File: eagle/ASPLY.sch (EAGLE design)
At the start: 69 parts, among them IC1 MC78L05ABP, IC2 TINY45, K1 Light, K2 Fan1, K3 Fan2, K4 Fan3, P1 MOLEX, T1 2SC1815, T2 2SC1815, T3 2SC1815, T4 2SC1815

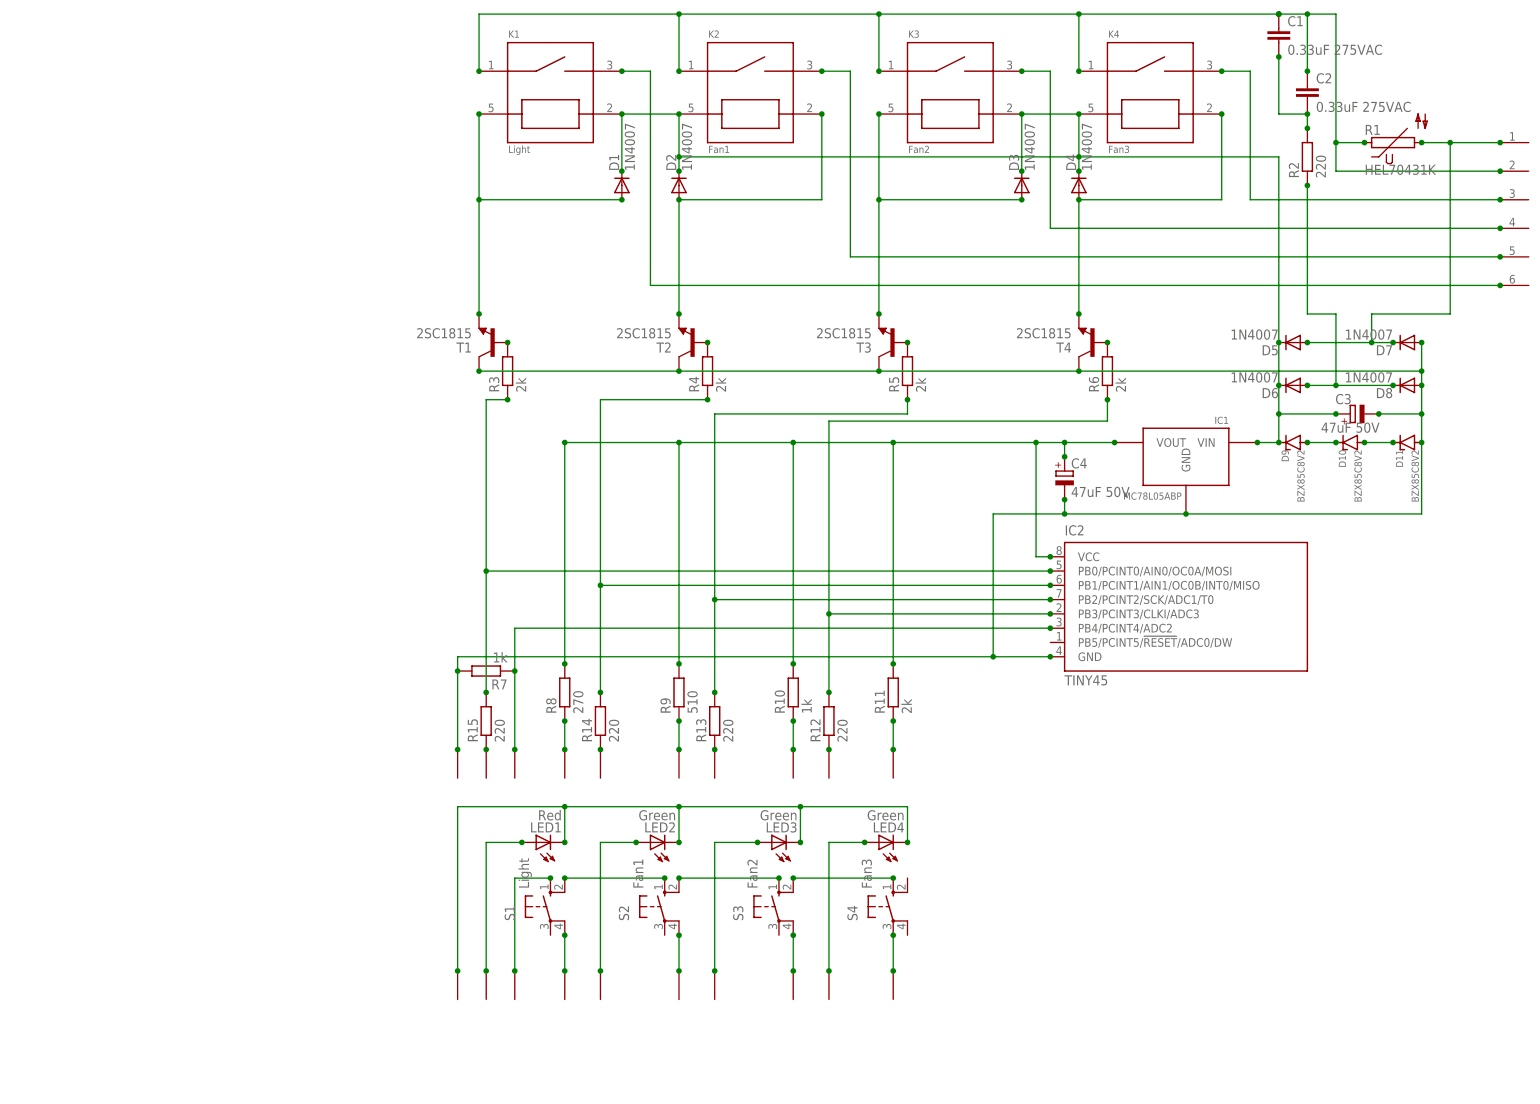
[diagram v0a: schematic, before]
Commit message: New HW revision:
- Split LED and transistor manage
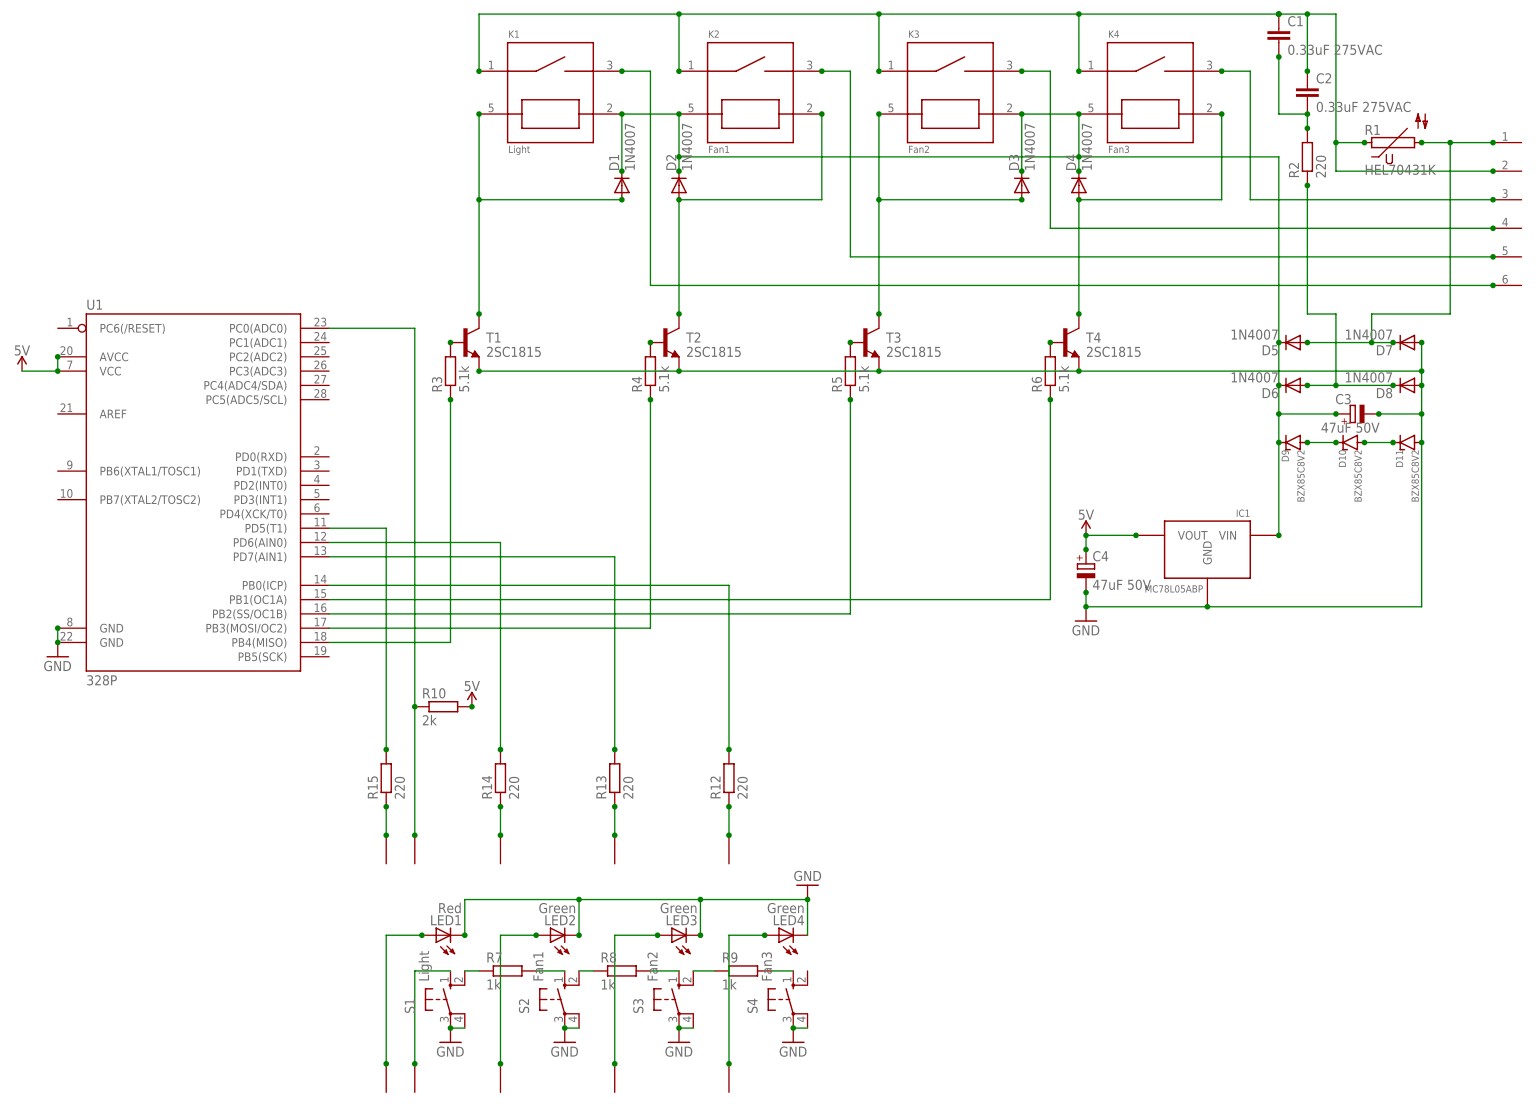
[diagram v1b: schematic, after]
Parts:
- removed IC2: TINY45, atmel:TINY13-20PU
- removed R11: 2k, rcl:R-EU_0204/7
- removed U$10, U$11, U$12, U$15, U$17, U$19, U$2, U$4, U$6, U$9: PIN, ASPLY:PIN
- added U1: 328P, SparkFun-IC-Microcontroller:ATMEGA328P_PDIP
- R10: value 1k -> 2k
- R3, R4, R5, R6: value 2k -> 5.1k
- R8: value 270 -> 1k
- R9: value 510 -> 1k
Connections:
- net N$1 renamed 220V
- net N$25 renamed LED_FAN3
- net N$26 renamed LED_FAN2
- net N$27 renamed LED_FAN1
- net N$28 renamed LED_LIGHT
- net N$6 renamed 0
- removed net N$29 (its old number): S3.S1, S4.S
- removed net N$30: LED1.C, LED2.C, LED3.C, LED4.C, U$11.1
- removed net N$31: S1.P1, U$19.1
- removed net N$32: S2.P1, U$17.1
- removed net N$33: S3.P1, U$15.1
- removed net N$34: S4.P, U$13.1
- removed net N$35: IC2.PB4/PCINT4/ADC2, R7.1, U$9.1
- removed net N$37: R11.1, U$2.1
- removed net N$39: R10.1, U$4.1
- removed net N$41: IC2.PB3/PCINT3/CLKI/ADC3, R12.2, R6.1
- removed net N$44: IC2.PB0/PCINT0/AIN0/OC0A/MOSI, R15.2, R3.1
- removed net N$45: R9.1, U$6.1
- removed net N$47: R8.1, U$8.1
- new net BUTTONS_INPUT: R10.1, U$8.1, U1.PC0(ADC0)
- new net LED_FAN1_OUTPUT: R14.2, U1.PD6(AIN0)
- new net LED_FAN2_OUTPUT: R13.2, U1.PD7(AIN1)
- new net LED_FAN3_OUTPUT: R12.2, U1.PB0(ICP)
- new net LED_LIGHT_OUTPUT: R15.2, U1.PD5(T1)
- new net N$1: S1.S, U$13.1
- new net N$15: R7.2, S2.S
- new net N$25: R9.2, S4.S
- new net N$6: R7.1, S1.S1
- new net N$7: R6.1, U1.PB1(OC1A)
- new net N$8: R5.1, U1.PB2(SS/OC1B)
- net 5V: now also U1.AVCC, U1.VCC; no longer IC2.VCC, R11.2, R8.2, R9.2
- net GND: now also LED1.C, LED2.C, LED3.C, LED4.C, S1.P, S1.P1, S2.P, S2.P1, S3.P, S3.P1, S4.P, S4.P1, T1.E, T2.E, T3.E, T4.E, U1.GND@1, U1.GND@2; no longer IC2.GND, R7.2, T1.C, T2.C, T3.C, T4.C, U$10.1
- net N$10: now also T2.C; no longer T2.E
- net N$11: now also T3.C; no longer T3.E
- net N$12: now also T4.C; no longer T4.E
- net N$22: now also R8.1, S2.S1; no longer S1.S1, S2.S
- net N$23: now also R8.2; no longer S2.S1
- net N$24: now also R9.1, S3.S1; no longer S1.S, U$12.1
- net N$42: now also R4.1, U1.PB3(MOSI/OC2); no longer IC2.PB2/PCINT2/SCK/ADC1/T0, R13.2, R5.1
- net N$43: now also R3.1, U1.PB4(MISO); no longer IC2.PB1/PCINT1/AIN1/OC0B/INT0/MISO, R14.2, R4.1
- net N$9: now also T1.C; no longer T1.E
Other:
- moved on the sheet: C4, IC1, LED1, LED2, LED3, LED4, R10, R12, R13, R14, R15, R3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

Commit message: Setup power supply
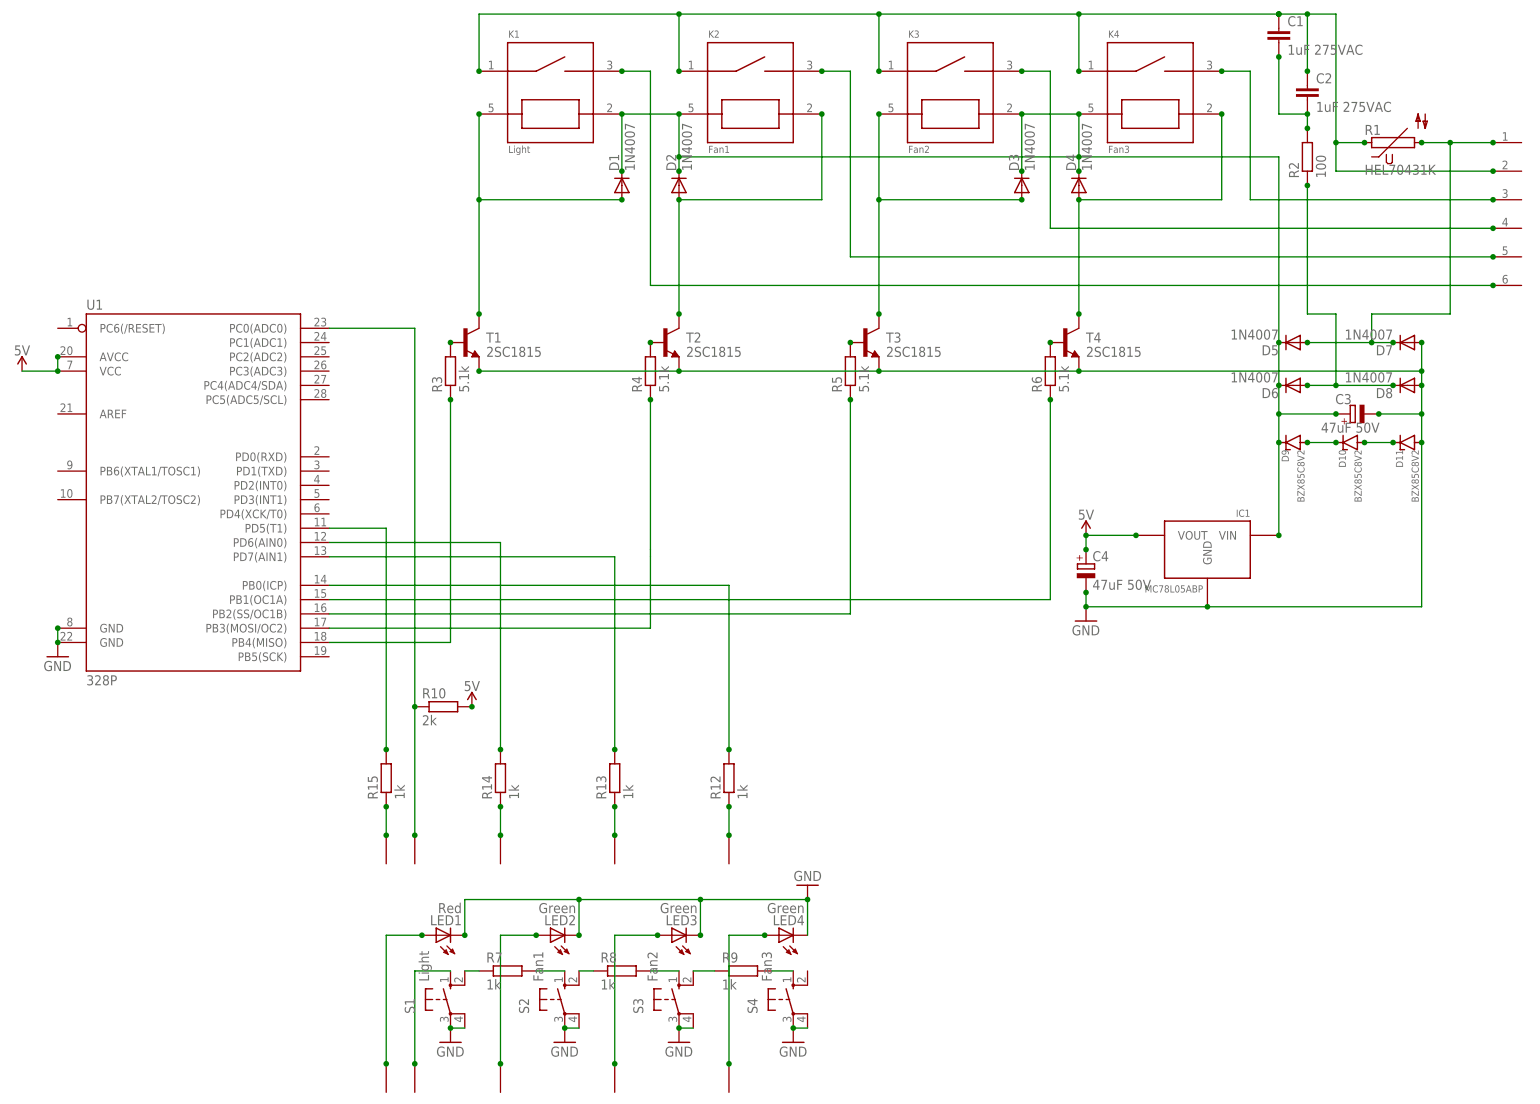
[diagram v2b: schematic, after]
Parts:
- C1, C2: value 0.33uF 275VAC -> 1uF 275VAC
- R12, R13, R14, R15: value 220 -> 1k
- R2: value 220 -> 100
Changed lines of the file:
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@@
 <setting verticaltext="up"/>
 </settings>
-<grid distance="0.05" unitdist="inch" unit="inch" style="lines" multiple="1" display="no" altdistance="0.01" altunitdist="inch" altunit="inch"/>
+<grid distance="0.1" unitdist="inch" unit="inch" style="lines" multiple="1" display="no" altdistance="0.01" altunitdist="inch" altunit="inch"/>
 <layers>
 <layer number="1" name="Top" color="4" fill="1" visible="no" active="no"/>
@@
 <part name="D7" library="diode" deviceset="1N4004" device="" value="1N4007"/>
 <part name="D8" library="diode" deviceset="1N4004" device="" value="1N4007"/>
-<part name="C1" library="capacitor-wima" deviceset="C" device="22/8" value="0.33uF 275VAC"/>
-<part name="C2" library="capacitor-wima" deviceset="C" device="22/8" value="0.33uF 275VAC"/>
-<part name="R2" library="resistor" deviceset="R-EU_" device="0617/22" value="220"/>
+<part name="C1" library="capacitor-wima" deviceset="C" device="22/8" value="1uF 275VAC"/>
+<part name="C2" library="capacitor-wima" deviceset="C" device="22/8" value="1uF 275VAC"/>
+<part name="R2" library="resistor" deviceset="R-EU_" device="0617/22" value="100"/>
 <part name="C3" library="rcl" deviceset="CPOL-EU" device="E5-6" value="47uF 50V"/>
 <part name="C4" library="rcl" deviceset="CPOL-EU" device="E5-6" value="47uF 50V"/>
@@
 <part name="R5" library="rcl" deviceset="R-EU_" device="0204/7" value="5.1k"/>
 <part name="R6" library="rcl" deviceset="R-EU_" device="0204/7" value="5.1k"/>
-<part name="R12" library="rcl" deviceset="R-EU_" device="0204/7" value="220"/>
-<part name="R13" library="rcl" deviceset="R-EU_" device="0204/7" value="220"/>
-<part name="R14" library="rcl" deviceset="R-EU_" device="0204/7" value="220"/>
-<part name="R15" library="rcl" deviceset="R-EU_" device="0204/7" value="220"/>
+<part name="R12" library="rcl" deviceset="R-EU_" device="0204/7" value="1k"/>
+<part name="R13" library="rcl" deviceset="R-EU_" device="0204/7" value="1k"/>
+<part name="R14" library="rcl" deviceset="R-EU_" device="0204/7" value="1k"/>
+<part name="R15" library="rcl" deviceset="R-EU_" device="0204/7" value="1k"/>
 <part name="U$1" library="ASPLY" deviceset="PIN" device=""/>
 <part name="U$3" library="ASPLY" deviceset="PIN" device=""/>
